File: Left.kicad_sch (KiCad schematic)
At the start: 27 parts, among them J5 Conn_01x02, U1 LM1117-3.3, U10 RP2040, U8 W25Q128JVS, Y2 ECS-120-8-33-JGN-TR3

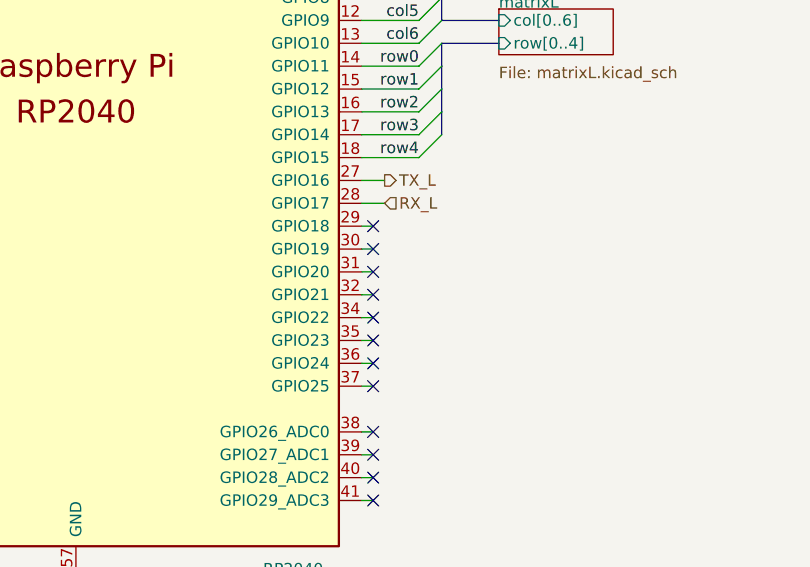
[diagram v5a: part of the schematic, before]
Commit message: Finished layout (for now), board outline, and new trrs jacks
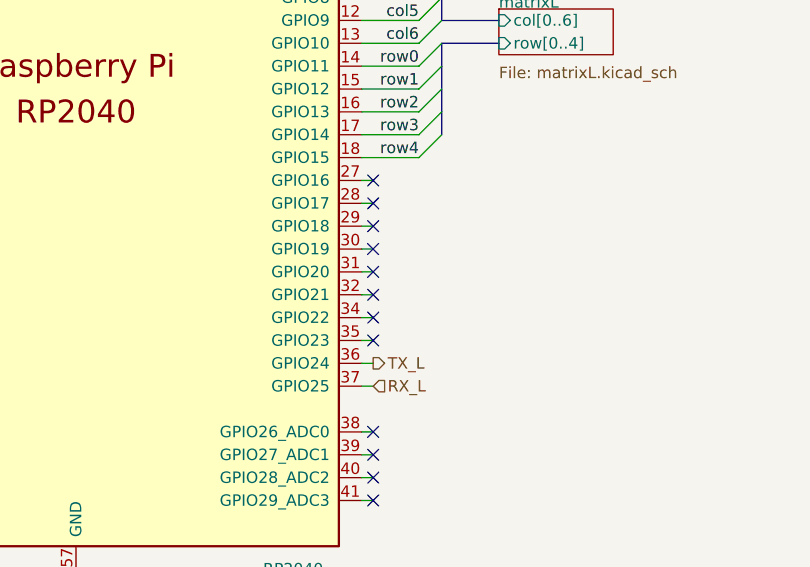
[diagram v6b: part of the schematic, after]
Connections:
- net RX_L: now also U10.37 (GPIO25); no longer U10.28 (GPIO17)
- net TX_L: now also U10.36 (GPIO24); no longer U10.27 (GPIO16)
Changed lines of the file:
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@@
   )
   (no_connect (at 201.93 154.94))
-  (no_connect (at 201.93 124.46))
   (no_connect (at 200.66 96.52))
   (no_connect (at 201.93 147.32))
-  (no_connect (at 201.93 129.54))
   (no_connect (at 201.93 127))
   (no_connect (at 200.66 78.74))
-  (no_connect (at 201.93 139.7))
   (no_connect (at 201.93 149.86))
+  (no_connect (at 201.93 129.54))
+  (no_connect (at 201.93 132.08))
   (no_connect (at 201.93 137.16))
   (no_connect (at 200.66 83.82))
+  (no_connect (at 201.93 124.46))
+  (no_connect (at 201.93 121.92))
+  (no_connect (at 201.93 119.38))
   (no_connect (at 200.66 81.28))
   (no_connect (at 201.93 152.4))
-  (no_connect (at 201.93 142.24))
-  (no_connect (at 201.93 132.08))
   (no_connect (at 201.93 134.62))
   (bus_entry (at 209.55 88.9) (size -2.54 2.54)
@@
     (stroke (width 0) (type default) (color 0 0 0 0))
   )
-  (wire (pts (xy 203.2 119.38) (xy 200.66 119.38))
-    (stroke (width 0) (type default) (color 0 0 0 0))
-  )
   (wire (pts (xy 200.66 106.68) (xy 207.01 106.68))
     (stroke (width 0) (type default) (color 0 0 0 0))
@@
     (stroke (width 0) (type default) (color 0 0 0 0))
   )
-  (wire (pts (xy 203.2 121.92) (xy 200.66 121.92))
-    (stroke (width 0) (type default) (color 0 0 0 0))
-  )
   (wire (pts (xy 73.66 77.47) (xy 73.66 81.28))
     (stroke (width 0) (type default) (color 0 0 0 0))
@@
     (stroke (width 0) (type default) (color 0 0 0 0))
   )
+  (wire (pts (xy 200.66 132.08) (xy 201.93 132.08))
+    (stroke (width 0) (type default) (color 0 0 0 0))
+  )
   (wire (pts (xy 185.42 48.26) (xy 185.42 60.96))
     (stroke (width 0) (type default) (color 0 0 0 0))
@@
     (stroke (width 0) (type default) (color 0 0 0 0))
   )
+  (wire (pts (xy 200.66 121.92) (xy 201.93 121.92))
+    (stroke (width 0) (type default) (color 0 0 0 0))
+  )
+  (wire (pts (xy 200.66 129.54) (xy 201.93 129.54))
+    (stroke (width 0) (type default) (color 0 0 0 0))
+  )
   (wire (pts (xy 45.72 153.67) (xy 77.47 153.67))
     (stroke (width 0) (type default) (color 0 0 0 0))
@@
     (stroke (width 0) (type default) (color 0 0 0 0))
   )
-  (wire (pts (xy 201.93 132.08) (xy 200.66 132.08))
-    (stroke (width 0) (type default) (color 0 0 0 0))
-  )
   (wire (pts (xy 200.66 139.7) (xy 201.93 139.7))
     (stroke (width 0) (type default) (color 0 0 0 0))
@@
     (stroke (width 0) (type default) (color 0 0 0 0))
   )
+  (wire (pts (xy 200.66 119.38) (xy 201.93 119.38))
+    (stroke (width 0) (type default) (color 0 0 0 0))
+  )
   (bus (pts (xy 209.55 104.14) (xy 215.9 104.14))
     (stroke (width 0) (type default) (color 0 0 0 0))
@@
   )
   (wire (pts (xy 80.01 77.47) (xy 73.66 77.47))
-    (stroke (width 0) (type default) (color 0 0 0 0))
-  )
-  (wire (pts (xy 201.93 129.54) (xy 200.66 129.54))
     (stroke (width 0) (type default) (color 0 0 0 0))
   )
@@
     (effects (font (size 1.27 1.27)) (justify left))
   )
-  (hierarchical_label "TX_L" (shape output) (at 203.2 119.38 0)
+  (hierarchical_label "TX_L" (shape output) (at 201.93 139.7 0)
     (effects (font (size 1.27 1.27)) (justify left))
   )
@@
     (effects (font (size 1.27 1.27)) (justify left))
   )
-  (hierarchical_label "RX_L" (shape input) (at 203.2 121.92 0)
+  (hierarchical_label "RX_L" (shape input) (at 201.93 142.24 0)
     (effects (font (size 1.27 1.27)) (justify left))
   )

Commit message: Started work on e.eco case cutout
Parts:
- added H1, H3, H4: MountingHole_Pad, MountingHole:MountingHole_3.2mm_M3_Pad_Via, symbol Mechanical:MountingHole_Pad
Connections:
- net GND_L: now also H1.1, H3.1, H4.1
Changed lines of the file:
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@@
     (pin "2")
+  )
+  (symbol (lib_id "Mechanical:MountingHole_Pad") (at 154.94 187.96 0) (unit 1)
+    (in_bom yes) (on_board yes) (fields_autoplaced)
+    (property "Reference" "H4" (id 0) (at 157.48 185.8553 0)
+      (effects (font (size 1.27 1.27)) (justify left))
+    )
+    (property "Value" "MountingHole_Pad" (id 1) (at 157.48 188.3922 0)
+      (effects (font (size 1.27 1.27)) (justify left))
+    )
+    (property "Footprint" "MountingHole:MountingHole_3.2mm_M3_Pad_Via" (id 2) (at 154.94 187.96 0)
+      (effects (font (size 1.27 1.27)) hide)
+    )
+    (property "Datasheet" "~" (id 3) (at 154.94 187.96 0)
+      (effects (font (size 1.27 1.27)) hide)
+    )
+    (pin "1")
   )
   (symbol (lib_id "Device:R") (at 63.5 163.83 270) (unit 1)
@@
     (pin "2")
   )
+  (symbol (lib_id "arisu-split:GND_L") (at 132.08 177.8 0) (unit 1)
+    (in_bom yes) (on_board yes) (fields_autoplaced)
+    (property "Reference" "#PWR0153" (id 0) (at 132.08 184.15 0)
+      (effects (font (size 1.27 1.27)) hide)
+    )
+    (property "Value" "GND_L" (id 1) (at 132.08 182.2434 0))
+    (property "Footprint" "" (id 2) (at 132.08 177.8 0)
+      (effects (font (size 1.27 1.27)) hide)
+    )
+    (property "Datasheet" "" (id 3) (at 132.08 177.8 0)
+      (effects (font (size 1.27 1.27)) hide)
+    )
+    (pin "1")
+  )
   (symbol (lib_id "arisu-split:GND_L") (at 128.27 39.37 0) (unit 1)
     (in_bom yes) (on_board yes) (fields_autoplaced)
@@
     (pin "1")
     (pin "2")
+  )
+  (symbol (lib_id "arisu-split:GND_L") (at 154.94 190.5 0) (unit 1)
+    (in_bom yes) (on_board yes) (fields_autoplaced)
+    (property "Reference" "#PWR0108" (id 0) (at 154.94 196.85 0)
+      (effects (font (size 1.27 1.27)) hide)
+    )
+    (property "Value" "GND_L" (id 1) (at 154.94 194.9434 0))
+    (property "Footprint" "" (id 2) (at 154.94 190.5 0)
+      (effects (font (size 1.27 1.27)) hide)
+    )
+    (property "Datasheet" "" (id 3) (at 154.94 190.5 0)
+      (effects (font (size 1.27 1.27)) hide)
+    )
+    (pin "1")
+  )
+  (symbol (lib_id "Mechanical:MountingHole_Pad") (at 132.08 187.96 0) (unit 1)
+    (in_bom yes) (on_board yes)
+    (property "Reference" "H3" (id 0) (at 134.62 185.8553 0)
+      (effects (font (size 1.27 1.27)) (justify left))
+    )
+    (property "Value" "MountingHole_Pad" (id 1) (at 134.62 188.3922 0)
+      (effects (font (size 1.27 1.27)) (justify left))
+    )
+    (property "Footprint" "MountingHole:MountingHole_3.2mm_M3_Pad_Via" (id 2) (at 132.08 187.96 0)
+      (effects (font (size 1.27 1.27)) hide)
+    )
+    (property "Datasheet" "~" (id 3) (at 132.08 187.96 0)
+      (effects (font (size 1.27 1.27)) hide)
+    )
+    (pin "1")
   )
   (symbol (lib_id "Device:C") (at 80.01 82.55 0) (unit 1)
@@
     (pin "4")
   )
+  (symbol (lib_id "Mechanical:MountingHole_Pad") (at 132.08 175.26 0) (unit 1)
+    (in_bom yes) (on_board yes) (fields_autoplaced)
+    (property "Reference" "H1" (id 0) (at 134.62 173.1553 0)
+      (effects (font (size 1.27 1.27)) (justify left))
+    )
+    (property "Value" "MountingHole_Pad" (id 1) (at 134.62 175.6922 0)
+      (effects (font (size 1.27 1.27)) (justify left))
+    )
+    (property "Footprint" "MountingHole:MountingHole_3.2mm_M3_Pad_Via" (id 2) (at 132.08 175.26 0)
+      (effects (font (size 1.27 1.27)) hide)
+    )
+    (property "Datasheet" "~" (id 3) (at 132.08 175.26 0)
+      (effects (font (size 1.27 1.27)) hide)
+    )
+    (pin "1")
+  )
   (symbol (lib_id "arisu-split:GND_L") (at 85.09 87.63 0) (unit 1)
     (in_bom yes) (on_board yes) (fields_autoplaced)
@@
       (effects (font (size 1.27 1.27)) hide)
     )
+    (pin "1")
+  )
+  (symbol (lib_id "arisu-split:GND_L") (at 132.08 190.5 0) (unit 1)
+    (in_bom yes) (on_board yes) (fields_autoplaced)
+    (property "Reference" "#PWR0151" (id 0) (at 132.08 196.85 0)
+      (effects (font (size 1.27 1.27)) hide)
+    )
+    (property "Value" "GND_L" (id 1) (at 132.08 194.9434 0))
+    (property "Footprint" "" (id 2) (at 132.08 190.5 0)
+      (effects (font (size 1.27 1.27)) hide)
+    )
+    (property "Datasheet" "" (id 3) (at 132.08 190.5 0)
+      (effects (font (size 1.27 1.27)) hide)
+    )

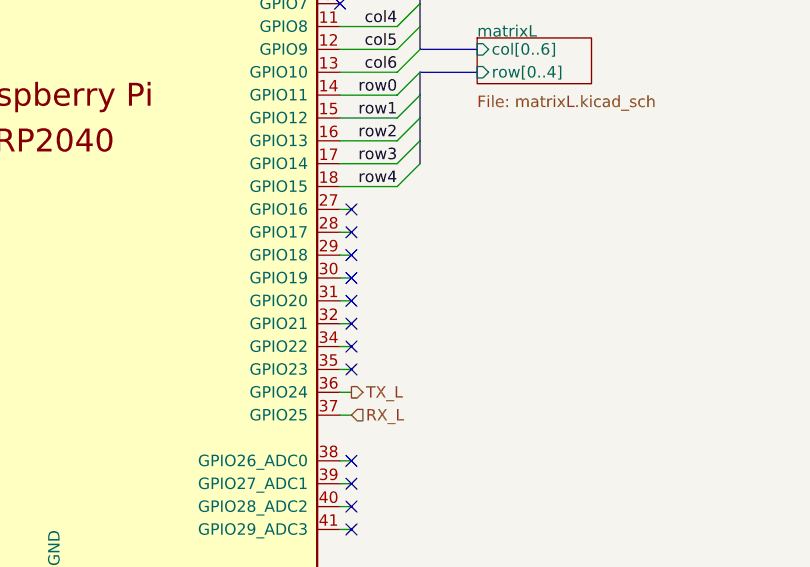
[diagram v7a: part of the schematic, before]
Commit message: left side of keyboard finished for the time being
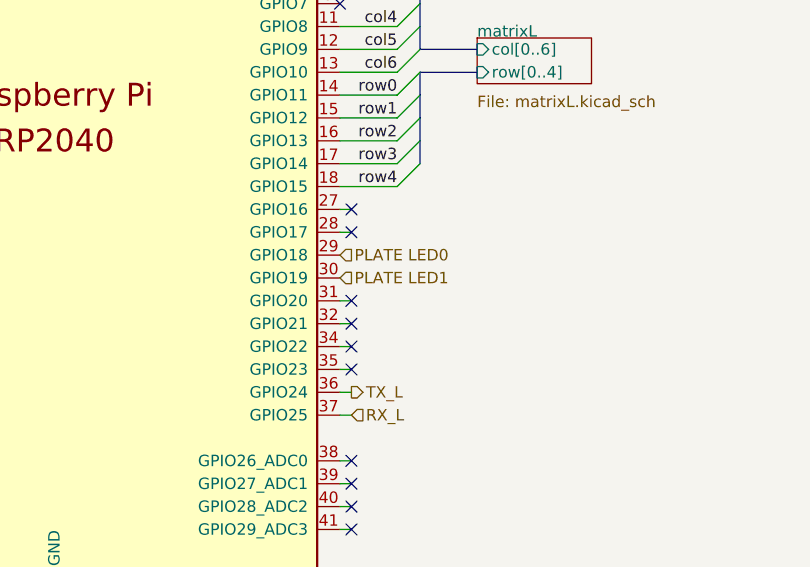
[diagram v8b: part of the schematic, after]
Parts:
- J5: footprint Connector_PinHeader_2.54mm:PinHeader_1x02_P2.54mm_Vertical -> Connector_PinHeader_2.54mm:PinHeader_1x02_P2.54mm_Horizontal
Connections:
- net PLATE LED0: now reaches U10.29 (GPIO18)
- net PLATE  LED1: now reaches U10.30 (GPIO19)
- no-connect marks 16 -> 14
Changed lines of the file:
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@@
   (no_connect (at 200.66 96.52))
   (no_connect (at 201.93 147.32))
-  (no_connect (at 201.93 127))
+  (no_connect (at 201.93 132.08))
   (no_connect (at 200.66 78.74))
   (no_connect (at 201.93 149.86))
+  (no_connect (at 201.93 137.16))
   (no_connect (at 201.93 129.54))
-  (no_connect (at 201.93 132.08))
-  (no_connect (at 201.93 137.16))
   (no_connect (at 200.66 83.82))
-  (no_connect (at 201.93 124.46))
+  (no_connect (at 201.93 134.62))
   (no_connect (at 201.93 121.92))
   (no_connect (at 201.93 119.38))
   (no_connect (at 200.66 81.28))
   (no_connect (at 201.93 152.4))
-  (no_connect (at 201.93 134.62))
   (bus_entry (at 209.55 88.9) (size -2.54 2.54)
     (stroke (width 0) (type default) (color 0 0 0 0))
@@
     (stroke (width 0) (type default) (color 0 0 0 0))
   )
+  (wire (pts (xy 201.93 134.62) (xy 200.66 134.62))
+    (stroke (width 0) (type default) (color 0 0 0 0))
+  )
   (wire (pts (xy 200.66 106.68) (xy 207.01 106.68))
     (stroke (width 0) (type default) (color 0 0 0 0))
@@
     (stroke (width 0) (type default) (color 0 0 0 0))
   )
+  (wire (pts (xy 128.27 29.21) (xy 128.27 27.94))
+    (stroke (width 0) (type default) (color 0 0 0 0))
+  )
+  (wire (pts (xy 205.74 36.83) (xy 205.74 39.37))
+    (stroke (width 0) (type default) (color 0 0 0 0))
+  )
+  (wire (pts (xy 170.18 48.26) (xy 172.72 48.26))
+    (stroke (width 0) (type default) (color 0 0 0 0))
+  )
+  (bus (pts (xy 209.55 109.22) (xy 209.55 111.76))
+    (stroke (width 0) (type default) (color 0 0 0 0))
+  )
+  (wire (pts (xy 160.02 60.96) (xy 160.02 48.26))
+    (stroke (width 0) (type default) (color 0 0 0 0))
+  )
+  (wire (pts (xy 262.89 39.37) (xy 262.89 40.64))
+    (stroke (width 0) (type default) (color 0 0 0 0))
+  )
+  (wire (pts (xy 185.42 48.26) (xy 185.42 60.96))
+    (stroke (width 0) (type default) (color 0 0 0 0))
+  )
+  (wire (pts (xy 58.42 101.6) (xy 60.96 101.6))
+    (stroke (width 0) (type default) (color 0 0 0 0))
+  )
+  (wire (pts (xy 27.94 104.14) (xy 27.94 105.41))
+    (stroke (width 0) (type default) (color 0 0 0 0))
+  )
+  (wire (pts (xy 168.91 162.56) (xy 168.91 165.1))
+    (stroke (width 0) (type default) (color 0 0 0 0))
+  )
+  (bus (pts (xy 209.55 101.6) (xy 215.9 101.6))
+    (stroke (width 0) (type default) (color 0 0 0 0))
+  )
+  (wire (pts (xy 240.03 29.21) (xy 240.03 27.94))
+    (stroke (width 0) (type default) (color 0 0 0 0))
+  )
+  (wire (pts (xy 205.74 27.94) (xy 217.17 27.94))
+    (stroke (width 0) (type default) (color 0 0 0 0))
+  )
+  (wire (pts (xy 34.29 153.67) (xy 45.72 153.67))
+    (stroke (width 0) (type default) (color 0 0 0 0))
+  )
+  (wire (pts (xy 228.6 36.83) (xy 228.6 39.37))
+    (stroke (width 0) (type default) (color 0 0 0 0))
+  )
+  (wire (pts (xy 185.42 43.18) (xy 185.42 48.26))
+    (stroke (width 0) (type default) (color 0 0 0 0))
+  )
+  (wire (pts (xy 137.16 132.08) (xy 134.62 132.08))
+    (stroke (width 0) (type default) (color 0 0 0 0))
+  )
+  (wire (pts (xy 217.17 29.21) (xy 217.17 27.94))
+    (stroke (width 0) (type default) (color 0 0 0 0))
+  )
+  (wire (pts (xy 185.42 26.67) (xy 185.42 27.94))
+    (stroke (width 0) (type default) (color 0 0 0 0))
+  )
+  (wire (pts (xy 201.93 132.08) (xy 200.66 132.08))
+    (stroke (width 0) (type default) (color 0 0 0 0))
+  )
+  (wire (pts (xy 139.7 43.18) (xy 148.59 43.18))
+    (stroke (width 0) (type default) (color 0 0 0 0))
+  )
   (wire (pts (xy 201.93 137.16) (xy 200.66 137.16))
     (stroke (width 0) (type default) (color 0 0 0 0))
   )
-  (wire (pts (xy 128.27 29.21) (xy 128.27 27.94))
-    (stroke (width 0) (type default) (color 0 0 0 0))
-  )
-  (wire (pts (xy 205.74 36.83) (xy 205.74 39.37))
-    (stroke (width 0) (type default) (color 0 0 0 0))
-  )
-  (wire (pts (xy 170.18 48.26) (xy 172.72 48.26))
-    (stroke (width 0) (type default) (color 0 0 0 0))
-  )
-  (bus (pts (xy 209.55 109.22) (xy 209.55 111.76))
-    (stroke (width 0) (type default) (color 0 0 0 0))
-  )
-  (wire (pts (xy 160.02 60.96) (xy 160.02 48.26))
-    (stroke (width 0) (type default) (color 0 0 0 0))
-  )
-  (wire (pts (xy 262.89 39.37) (xy 262.89 40.64))
-    (stroke (width 0) (type default) (color 0 0 0 0))
-  )
-  (wire (pts (xy 201.93 134.62) (xy 200.66 134.62))
-    (stroke (width 0) (type default) (color 0 0 0 0))
-  )
-  (wire (pts (xy 200.66 132.08) (xy 201.93 132.08))
-    (stroke (width 0) (type default) (color 0 0 0 0))
-  )
-  (wire (pts (xy 185.42 48.26) (xy 185.42 60.96))
-    (stroke (width 0) (type default) (color 0 0 0 0))
-  )
-  (wire (pts (xy 58.42 101.6) (xy 60.96 101.6))
-    (stroke (width 0) (type default) (color 0 0 0 0))
-  )
-  (wire (pts (xy 27.94 104.14) (xy 27.94 105.41))
-    (stroke (width 0) (type default) (color 0 0 0 0))
-  )
-  (wire (pts (xy 200.66 124.46) (xy 201.93 124.46))
-    (stroke (width 0) (type default) (color 0 0 0 0))
-  )
-  (wire (pts (xy 168.91 162.56) (xy 168.91 165.1))
-    (stroke (width 0) (type default) (color 0 0 0 0))
-  )
-  (bus (pts (xy 209.55 101.6) (xy 215.9 101.6))
-    (stroke (width 0) (type default) (color 0 0 0 0))
-  )
-  (wire (pts (xy 240.03 29.21) (xy 240.03 27.94))
-    (stroke (width 0) (type default) (color 0 0 0 0))
-  )
-  (wire (pts (xy 205.74 27.94) (xy 217.17 27.94))
-    (stroke (width 0) (type default) (color 0 0 0 0))
-  )
-  (wire (pts (xy 34.29 153.67) (xy 45.72 153.67))
-    (stroke (width 0) (type default) (color 0 0 0 0))
-  )
-  (wire (pts (xy 228.6 36.83) (xy 228.6 39.37))
-    (stroke (width 0) (type default) (color 0 0 0 0))
-  )
-  (wire (pts (xy 185.42 43.18) (xy 185.42 48.26))
-    (stroke (width 0) (type default) (color 0 0 0 0))
-  )
-  (wire (pts (xy 137.16 132.08) (xy 134.62 132.08))
-    (stroke (width 0) (type default) (color 0 0 0 0))
-  )
-  (wire (pts (xy 217.17 29.21) (xy 217.17 27.94))
-    (stroke (width 0) (type default) (color 0 0 0 0))
-  )
-  (wire (pts (xy 185.42 26.67) (xy 185.42 27.94))
-    (stroke (width 0) (type default) (color 0 0 0 0))
-  )
-  (wire (pts (xy 139.7 43.18) (xy 148.59 43.18))
-    (stroke (width 0) (type default) (color 0 0 0 0))
-  )
   (wire (pts (xy 151.13 60.96) (xy 151.13 48.26))
     (stroke (width 0) (type default) (color 0 0 0 0))
@@
   )
   (wire (pts (xy 200.66 88.9) (xy 207.01 88.9))
-    (stroke (width 0) (type default) (color 0 0 0 0))
-  )
-  (wire (pts (xy 200.66 127) (xy 201.93 127))
     (stroke (width 0) (type default) (color 0 0 0 0))
   )
@@
   )
   (hierarchical_label "TX_L" (shape output) (at 201.93 139.7 0)
+    (effects (font (size 1.27 1.27)) (justify left))
+  )
+  (hierarchical_label "PLATE LED0" (shape input) (at 200.66 124.46 0)
+    (effects (font (size 1.27 1.27)) (justify left))
+  )
+  (hierarchical_label "PLATE  LED1" (shape input) (at 200.66 127 0)
     (effects (font (size 1.27 1.27)) (justify left))
   )
@@
     (property "Reference" "J5" (id 0) (at 20.32 97.79 0))
     (property "Value" "Conn_01x02" (id 1) (at 20.32 107.95 0))
-    (property "Footprint" "Connector_PinHeader_2.54mm:PinHeader_1x02_P2.54mm_Vertical" (id 2) (at 21.59 101.6 0)
-      (effects (font (size 1.27 1.27)) hide)
-    )
+    (property "Footprint" "Connector_PinHeader_2.54mm:PinHeader_1x02_P2.54mm_Horizontal" (id 2) (at 21.59 101.6 0)
+      (effects (font (size 1.27 1.27)) hide)
+    )
